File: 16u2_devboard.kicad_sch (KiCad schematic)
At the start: 24 parts

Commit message: Assigned footprints
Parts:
- C2, C3: renamed from C?; value (none) -> 22p
- J3: renamed from J?; value (none) -> CONN_L
- J4: renamed from J?; value (none) -> CONN_R
- gave numbers to parts that had none: 20
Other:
- moved on the sheet: D1, D2, F1, J1, J2, J3, J4, R2, R3, R4, R5, RV1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

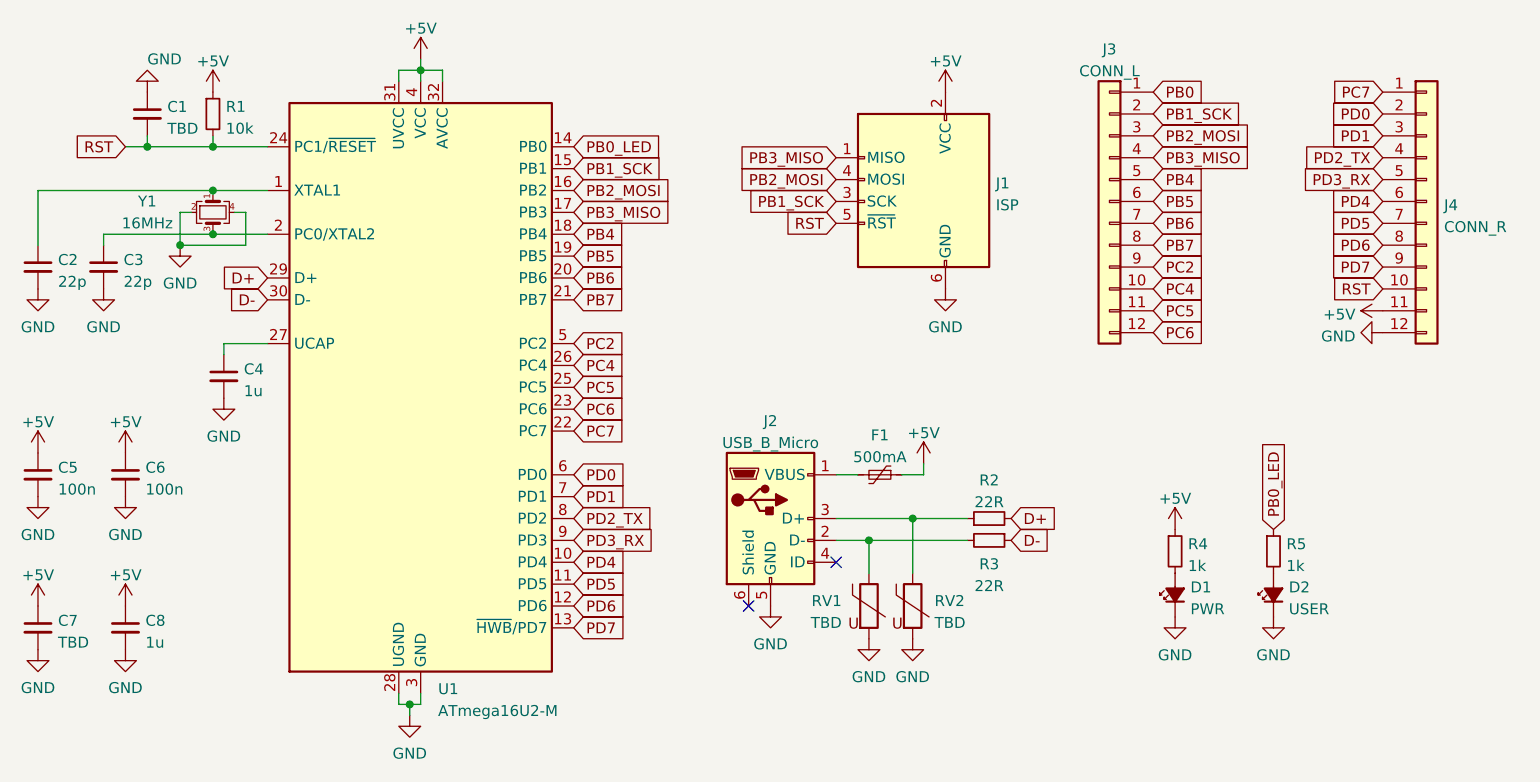
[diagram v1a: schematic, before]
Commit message: Loose layout created - Added netnames to schematic - Changed XTAL footprint
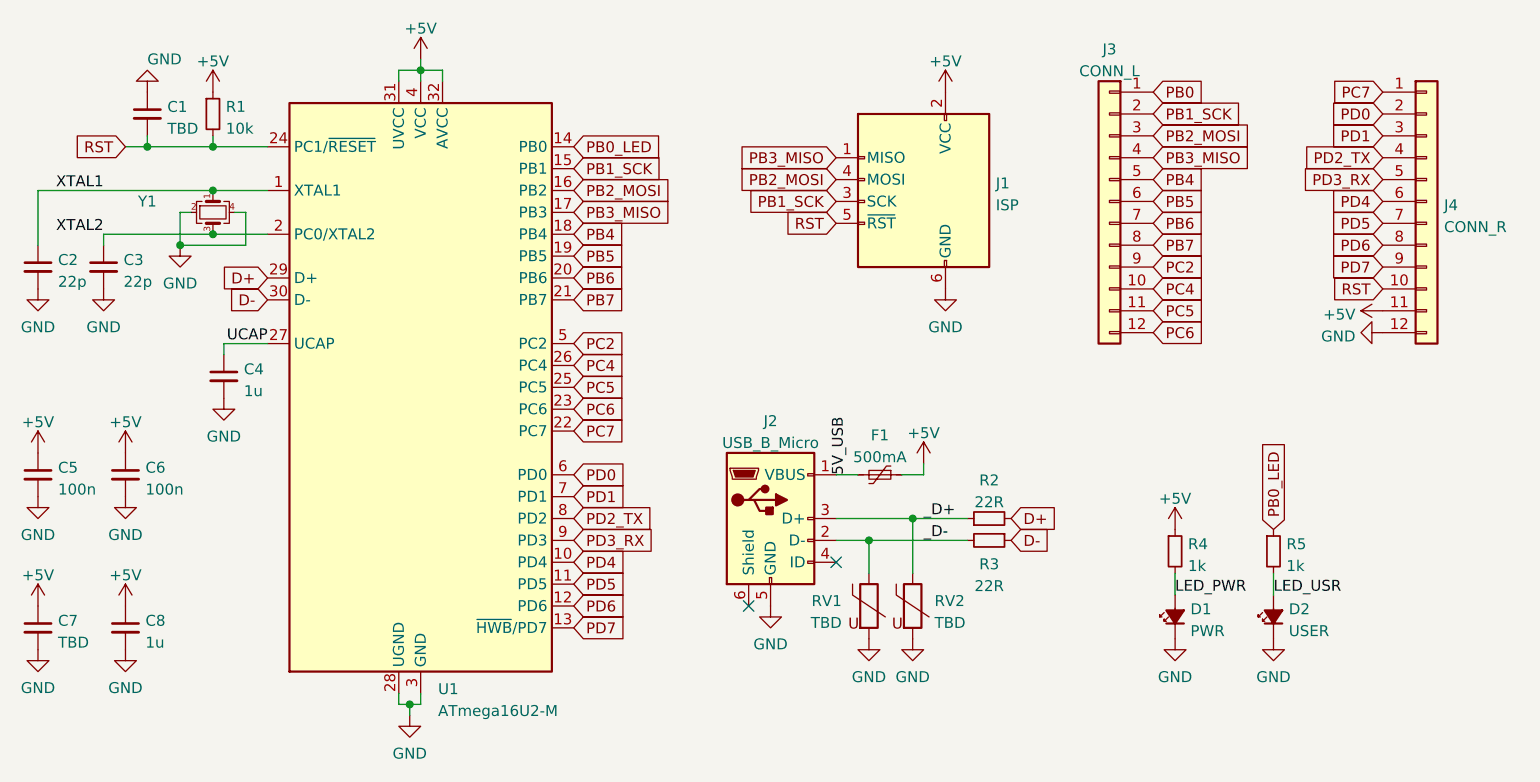
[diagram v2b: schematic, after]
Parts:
- C1, C2, C3, C5, C6: footprint (none) -> Capacitor_SMD:C_0402_1005Metric_Pad0.74x0.62mm_HandSolder
- C4, C8: footprint (none) -> Capacitor_SMD:C_0603_1608Metric_Pad1.08x0.95mm_HandSolder
- C7: footprint (none) -> Capacitor_SMD:C_1210_3225Metric_Pad1.33x2.70mm_HandSolder
- D1, D2: footprint (none) -> Diode_SMD:D_0603_1608Metric_Pad1.05x0.95mm_HandSolder
- F1: footprint (none) -> Fuse:Fuse_1812_4532Metric_Pad1.30x3.40mm_HandSolder
- J1: footprint (none) -> Connector_PinHeader_2.54mm:PinHeader_2x03_P2.54mm_Vertical
- J2: footprint (none) -> global:USB_MICRO_B_C456008
- J3, J4: footprint (none) -> Connector_PinHeader_2.54mm:PinHeader_1x12_P2.54mm_Vertical
- R1, R2, R3, R4, R5: footprint (none) -> Resistor_SMD:R_0402_1005Metric_Pad0.72x0.64mm_HandSolder
- RV1, RV2: footprint (none) -> Resistor_SMD:R_0603_1608Metric_Pad0.98x0.95mm_HandSolder
- Y1: value 16MHz -> (none)
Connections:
- net _D+: now reaches J2.3 (D+), R2.1, RV2.1
- net LED_PWR: now reaches D1.2 (A), R4.2
- net 5V_USB: now reaches F1.2, J2.1 (VBUS)
- net _D-: now reaches J2.2 (D-), R3.2, RV1.1
- net LED_USR: now reaches D2.2 (A), R5.2
- net XTAL1: now reaches C2.1, U1.1 (XTAL1), Y1.1
- net XTAL2: now reaches C3.1, U1.2 (PC0/XTAL2), Y1.3
- net UCAP: now reaches C4.1, U1.27 (UCAP)
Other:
- moved on the sheet: D1, D2

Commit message: v1.0 Finished - Layout and routing finished - Silkscreen markings added - Logo as part of ground pour
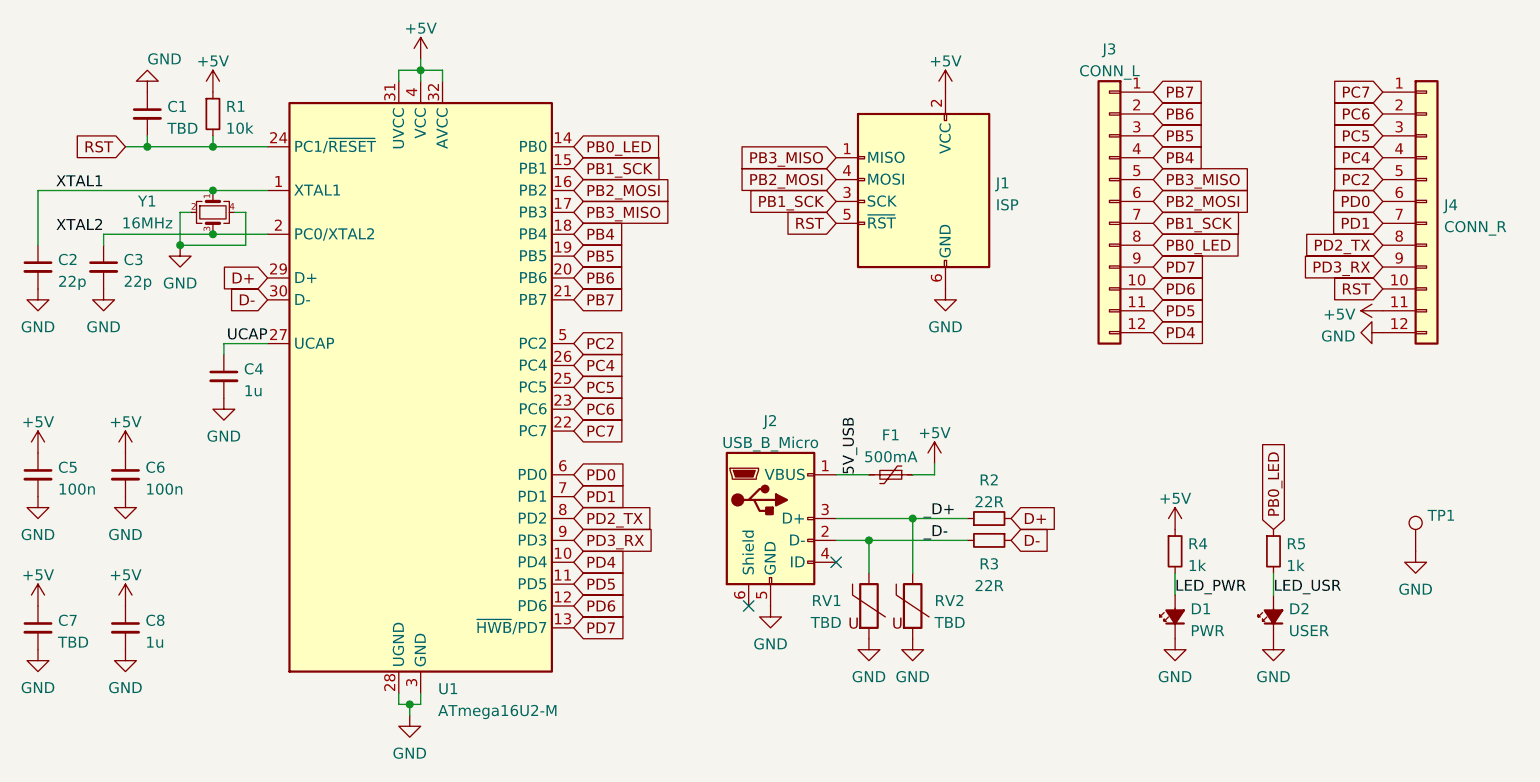
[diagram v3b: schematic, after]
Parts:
- added TP1: (no value), symbol Connector:TestPoint
- Y1: value (none) -> 16MHz; footprint (none) -> Crystal:Crystal_SMD_3225-4Pin_3.2x2.5mm
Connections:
- net PB0 is gone; now on net PB7: J3.1 (Pin_1)
- net GND: now also TP1.1
- net PB0_LED: now also J3.8 (Pin_8)
- net PB1_SCK: now also J3.7 (Pin_7); no longer J3.2 (Pin_2)
- net PB2_MOSI: now also J3.6 (Pin_6); no longer J3.3 (Pin_3)
- net PB3_MISO: now also J3.5 (Pin_5); no longer J3.4 (Pin_4)
- net PB4: now also J3.4 (Pin_4); no longer J3.5 (Pin_5)
- net PB5: now also J3.3 (Pin_3); no longer J3.6 (Pin_6)
- net PB6: now also J3.2 (Pin_2); no longer J3.7 (Pin_7)
- net PB7: no longer J3.8 (Pin_8)
- net PC2: now also J4.5 (Pin_5); no longer J3.9 (Pin_9)
- net PC4: now also J4.4 (Pin_4); no longer J3.10 (Pin_10)
- net PC5: now also J4.3 (Pin_3); no longer J3.11 (Pin_11)
- net PC6: now also J4.2 (Pin_2); no longer J3.12 (Pin_12)
- net PD0: now also J4.6 (Pin_6); no longer J4.2 (Pin_2)
- net PD1: now also J4.7 (Pin_7); no longer J4.3 (Pin_3)
- net PD2_TX: now also J4.8 (Pin_8); no longer J4.4 (Pin_4)
- net PD3_RX: now also J4.9 (Pin_9); no longer J4.5 (Pin_5)
- net PD4: now also J3.12 (Pin_12); no longer J4.6 (Pin_6)
- net PD5: now also J3.11 (Pin_11); no longer J4.7 (Pin_7)
- net PD6: now also J3.10 (Pin_10); no longer J4.8 (Pin_8)
- net PD7: now also J3.9 (Pin_9); no longer J4.9 (Pin_9)
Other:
- company: (none) -> aspyra
- title: (none) -> Mega16u2 devboard
- moved on the sheet: F1
